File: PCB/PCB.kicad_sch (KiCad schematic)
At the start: 54 parts, among them J1 USB_C_Receptacle_USB2.0_16P, Q2 IRLML2060, SW1 SW_Push, SW2 SW_Push, U1 RP2040, U2 USBLC6-2SC6, U3 NCP1117ST33T3G, U4 W25Q32JVSS, U5 Conn, Y1 Crystal_GND24

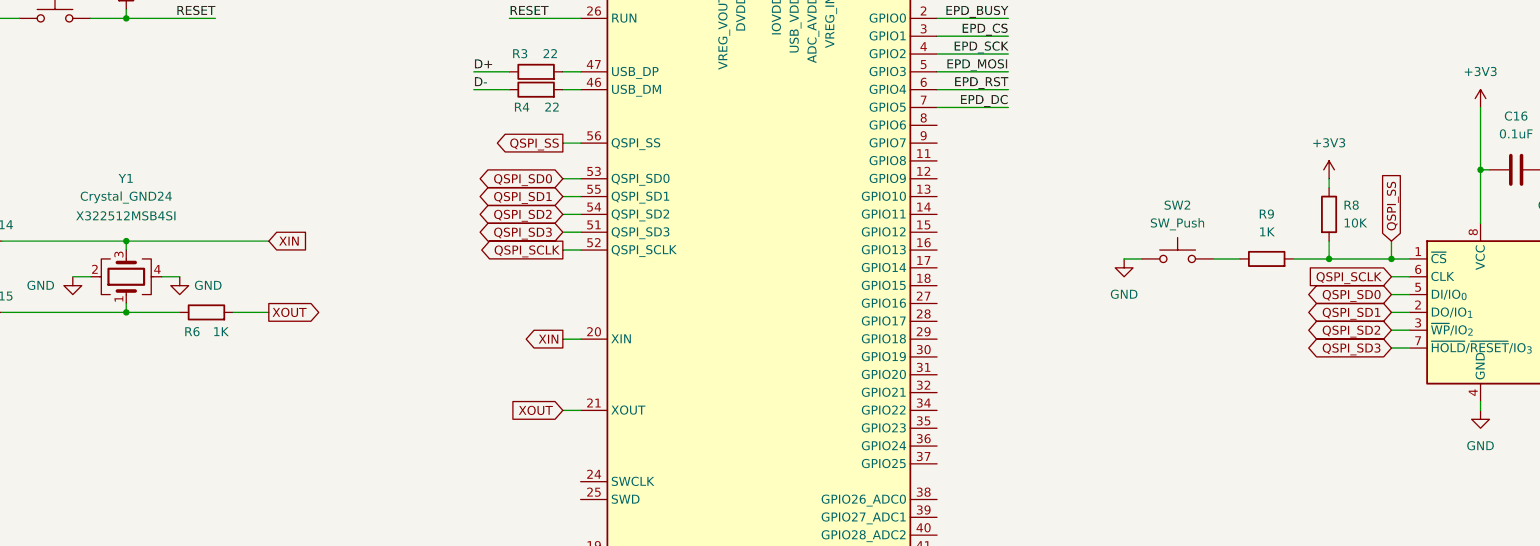
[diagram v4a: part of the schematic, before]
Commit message: changed all the global labels to net labels for funesies
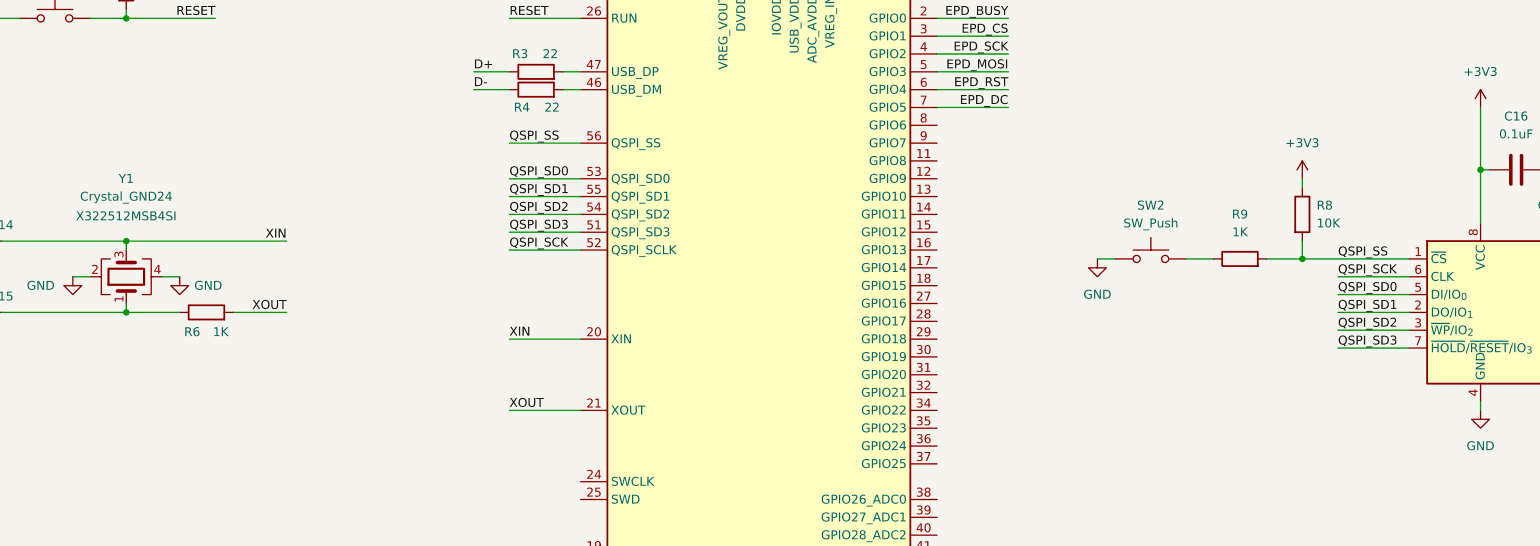
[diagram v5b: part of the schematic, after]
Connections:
- net QSPI_SCLK renamed QSPI_SCK
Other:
- moved on the sheet: R8, R9, SW2

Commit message: chose my NFC RFID IC
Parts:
- added U6: ST25DV04K-JFR6D3, Package_DFN_QFN:ST_UFDFPN-12-1EP_3x3mm_P0.5mm_EP1.4x2.55mm, symbol RF_NFC:ST25DV04K-JFR6D3
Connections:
- net GND: now also U1.19 (TESTEN), U6.6 (VSS)
- no-connect marks 4 -> 6

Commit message: wired the NFC RFID IC
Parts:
- added C29: 0.1uF, symbol Device:C
- added R10, R13, R14: 10K, symbol Device:R
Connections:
- net +3V3: now also U6.10 (VDCG), U6.12 (VCC), C29.2, R10.1, R13.1, R14.1
- net GND: now also C29.1
- net at U6.11 (GPO): now also R14.2
- net at U6.7 (SDA): now also R10.2
- net at U6.8 (SCL): now also R13.2
- no-connect marks 6 -> 8
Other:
- moved on the sheet: U6

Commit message: wiring NFC RFID to MCU
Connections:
- net NFC_GPO: now reaches U1.11 (GPIO8)
- net NFC_GPO: now also R14.2, U6.11 (GPO)
- net NFC_SDA: now reaches U1.8 (GPIO6)
- net NFC_SDA: now also R10.2, U6.7 (SDA)
- net NFC_SCL: now reaches U1.9 (GPIO7)
- net NFC_SCL: now also R13.2, U6.8 (SCL)
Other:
- note added: "Wired this because I had too many GPIO's and might as well give more user features!"
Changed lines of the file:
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@@
+		)
+	)
+	(text "Wired this because I had too many GPIO's \nand might as well give more user features!"
+		(exclude_from_sim no)
+		(at 354.584 28.956 0)
+		(effects
+			(font
+				(size 1.27 1.27)
+			)
 		)
 	)
@@
 	(wire
 		(pts
+			(xy 187.96 195.58) (xy 177.8 195.58)
+		)
+		(stroke
+			(width 0)
+			(type default)
+		)
+	)
+	(wire
+		(pts
 			(xy 236.22 69.85) (xy 233.68 69.85)
 		)
@@
 	(wire
 		(pts
-			(xy 375.92 60.96) (xy 387.35 60.96)
+			(xy 375.92 60.96) (xy 388.62 60.96)
 		)
 		(stroke
@@
 	(wire
 		(pts
+			(xy 187.96 190.5) (xy 177.8 190.5)
+		)
+		(stroke
+			(width 0)
+			(type default)
+		)
+	)
+	(wire
+		(pts
 			(xy 241.3 72.39) (xy 233.68 72.39)
 		)
@@
 	(wire
 		(pts
+			(xy 187.96 193.04) (xy 177.8 193.04)
+		)
+		(stroke
+			(width 0)
+			(type default)
+		)
+	)
+	(wire
+		(pts
 			(xy 212.09 54.61) (xy 203.2 54.61)
 		)
@@
 	(wire
 		(pts
-			(xy 318.77 60.96) (xy 323.85 60.96)
+			(xy 311.15 60.96) (xy 323.85 60.96)
 		)
 		(stroke
@@
 	(wire
 		(pts
-			(xy 318.77 58.42) (xy 332.74 58.42)
+			(xy 311.15 58.42) (xy 332.74 58.42)
 		)
 		(stroke
@@
 		)
 	)
+	(label "NFC_GPO"
+		(at 187.96 195.58 180)
+		(effects
+			(font
+				(size 1.27 1.27)
+			)
+			(justify right bottom)
+		)
+	)
 	(label "EPD_BUSY"
 		(at 248.92 46.99 0)
@@
 		)
 	)
+	(label "NFC_SDA"
+		(at 311.15 58.42 0)
+		(effects
+			(font
+				(size 1.27 1.27)
+			)
+			(justify left bottom)
+		)
+	)
+	(label "NFC_SDA"
+		(at 187.96 190.5 180)
+		(effects
+			(font
+				(size 1.27 1.27)
+			)
+			(justify right bottom)
+		)
+	)
 	(label "QSPI_SS"
 		(at 234.95 209.55 0)
@@
 		)
 	)
+	(label "NFC_SCL"
+		(at 187.96 193.04 180)
+		(effects
+			(font
+				(size 1.27 1.27)
+			)
+			(justify right bottom)
+		)
+	)
 	(label "QSPI_SD1"
 		(at 234.95 217.17 0)
@@
 		)
 	)
+	(label "NFC_SCL"
+		(at 311.15 60.96 0)
+		(effects
+			(font
+				(size 1.27 1.27)
+			)
+			(justify left bottom)
+		)
+	)
 	(label "RESE"
 		(at 248.92 31.75 0)
@@
 		)
 	)
+	(label "NFC_GPO"
+		(at 388.62 60.96 180)
+		(effects
+			(font
+				(size 1.27 1.27)
+			)
+			(justify right bottom)
+		)
+	)
